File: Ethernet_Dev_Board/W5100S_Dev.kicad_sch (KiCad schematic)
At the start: 41 parts, among them U302 74AUP1T08GWH, Y301 25MHz

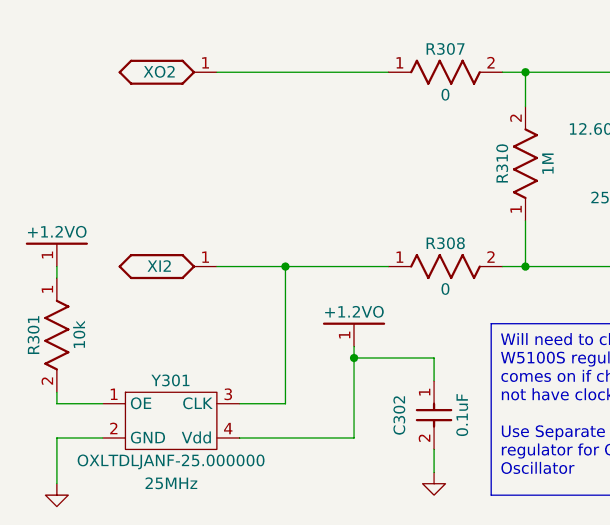
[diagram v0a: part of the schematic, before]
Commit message: Added in 1.2 V regulator and broke out unused IO pins to header
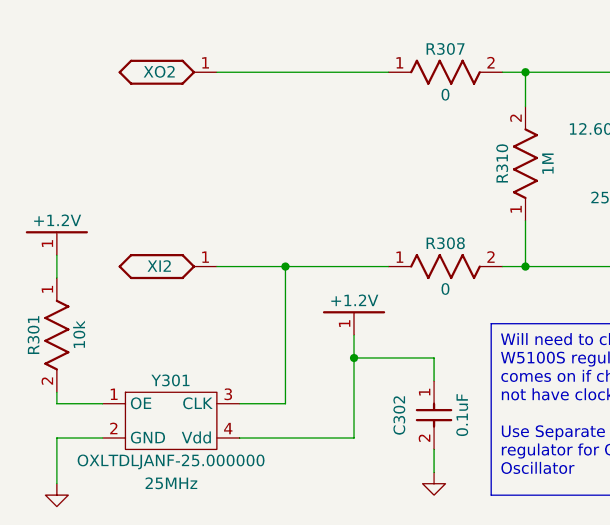
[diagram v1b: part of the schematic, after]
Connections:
- net +1.2VO: no longer C302.1, R301.1, Y301.4 (Vdd)
- new net +1.2V: C302.1, R301.1, Y301.4 (Vdd)
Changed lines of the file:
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@@
 	(wire
 		(pts
-			(xy 50.8 179.07) (xy 50.8 177.8)
+			(xy 50.8 176.53) (xy 50.8 179.07)
 		)
 		(stroke
@@
 	(wire
 		(pts
-			(xy 17.78 170.18) (xy 17.78 168.91)
+			(xy 17.78 167.64) (xy 17.78 170.18)
 		)
 		(stroke
@@
 	)
 	(symbol
+		(lib_id "LED_Controller_Hardware-eagle-import:+3.3V")
+		(at 50.8 177.8 0)
+		(unit 1)
+		(exclude_from_sim no)
+		(in_bom yes)
+		(on_board yes)
+		(dnp no)
+		(property "Reference" "#NetPort0308"
+			(at 50.8 177.8 0)
+			(effects
+				(font
+					(size 1.27 1.27)
+				)
+				(hide yes)
+			)
+		)
+		(property "Value" "+1.2V"
+			(at 50.8 172.72 0)
+			(effects
+				(font
+					(size 1.27 1.27)
+				)
+			)
+		)
+		(property "Footprint" ""
+			(at 50.8 177.8 0)
+			(effects
+				(font
+					(size 1.27 1.27)
+				)
+				(hide yes)
+			)
+		)
+		(property "Datasheet" ""
+			(at 50.8 177.8 0)
+			(effects
+				(font
+					(size 1.27 1.27)
+				)
+				(hide yes)
+			)
+		)
+		(property "Description" ""
+			(at 50.8 177.8 0)
+			(effects
+				(font
+					(size 1.27 1.27)
+				)
+				(hide yes)
+			)
+		)
+		(property "Mfg." ""
+			(at 50.8 177.8 0)
+			(effects
+				(font
+					(size 1.27 1.27)
+				)
+				(hide yes)
+			)
+		)
+		(property "Mfg. PN" ""
+			(at 50.8 177.8 0)
+			(effects
+				(font
+					(size 1.27 1.27)
+				)
+				(hide yes)
+			)
+		)
+		(property "Distributor" ""
+			(at 50.8 177.8 0)
+			(effects
+				(font
+					(size 1.27 1.27)
+				)
+				(hide yes)
+			)
+		)
+		(property "Distributor PN" ""
+			(at 50.8 177.8 0)
+			(effects
+				(font
+					(size 1.27 1.27)
+				)
+				(hide yes)
+			)
+		)
+		(pin "1"
+		)
+		(instances
+			(project "Ethernet_Dev_Board"
+				(path "/79118fbd-6cbf-48b1-af39-9f7b00f17642/e515d953-e2e5-40ce-8d77-bb09cabdad3d"
+					(reference "#NetPort0308")
+					(unit 1)
+				)
+			)
+		)
+	)
+	(symbol
 		(lib_id "LED_Controller_Hardware-eagle-import:ETH_EN")
 		(at 36.83 97.79 180)
@@
 	)
 	(symbol
-		(lib_id "LED_Controller_Hardware-eagle-import:+3.3VA")
-		(at 17.78 170.18 0)
-		(unit 1)
-		(exclude_from_sim no)
-		(in_bom yes)
-		(on_board yes)
-		(dnp no)
-		(property "Reference" "#NetPort0301"
-			(at 17.78 170.18 0)
-			(effects
-				(font
-					(size 1.27 1.27)
-				)
-				(hide yes)
-			)
-		)
-		(property "Value" "+1.2VO"
-			(at 17.78 165.1 0)
-			(effects
-				(font
-					(size 1.27 1.27)
-				)
-			)
-		)
-		(property "Footprint" ""
-			(at 17.78 170.18 0)
-			(effects
-				(font
-					(size 1.27 1.27)
-				)
-				(hide yes)
-			)
-		)
-		(property "Datasheet" ""
-			(at 17.78 170.18 0)
-			(effects
-				(font
-					(size 1.27 1.27)
-				)
-				(hide yes)
-			)
-		)
-		(property "Description" ""
-			(at 17.78 170.18 0)
-			(effects
-				(font
-					(size 1.27 1.27)
-				)
-				(hide yes)
-			)
-		)
-		(property "Mfg." ""
-			(at 17.78 170.18 0)
-			(effects
-				(font
-					(size 1.27 1.27)
-				)
-				(hide yes)
-			)
-		)
-		(property "Mfg. PN" ""
-			(at 17.78 170.18 0)
-			(effects
-				(font
-					(size 1.27 1.27)
-				)
-				(hide yes)
-			)
-		)
-		(property "Distributor" ""
-			(at 17.78 170.18 0)
-			(effects
-				(font
-					(size 1.27 1.27)
-				)
-				(hide yes)
-			)
-		)
-		(property "Distributor PN" ""
-			(at 17.78 170.18 0)
-			(effects
-				(font
-					(size 1.27 1.27)
-				)
-				(hide yes)
-			)
-		)
-		(pin "1"
-		)
-		(instances
-			(project "Ethernet_Dev_Board"
-				(path "/79118fbd-6cbf-48b1-af39-9f7b00f17642/e515d953-e2e5-40ce-8d77-bb09cabdad3d"
-					(reference "#NetPort0301")
-					(unit 1)
-				)
-			)
-		)
-	)
-	(symbol
 		(lib_id "power:GNDS")
 		(at 96.52 165.1 0)
@@
 	(symbol
 		(lib_id "LED_Controller_Hardware-eagle-import:+3.3VA")
-		(at 50.8 179.07 0)
-		(unit 1)
-		(exclude_from_sim no)
-		(in_bom yes)
-		(on_board yes)
-		(dnp no)
-		(property "Reference" "#NetPort0308"
-			(at 50.8 179.07 0)
-			(effects
-				(font
-					(size 1.27 1.27)
-				)
-				(hide yes)
-			)
-		)
-		(property "Value" "+1.2VO"
-			(at 50.8 173.99 0)
-			(effects
-				(font
-					(size 1.27 1.27)
-				)
-			)
-		)
-		(property "Footprint" ""
-			(at 50.8 179.07 0)
-			(effects
-				(font
-					(size 1.27 1.27)
-				)
-				(hide yes)
-			)
-		)
-		(property "Datasheet" ""
-			(at 50.8 179.07 0)
-			(effects
-				(font
-					(size 1.27 1.27)
-				)
-				(hide yes)
-			)
-		)
-		(property "Description" ""
-			(at 50.8 179.07 0)
-			(effects
-				(font
-					(size 1.27 1.27)
-				)
-				(hide yes)
-			)
-		)
-		(property "Mfg." ""
-			(at 50.8 179.07 0)
-			(effects
-				(font
-					(size 1.27 1.27)
-				)
-				(hide yes)
-			)
-		)
-		(property "Mfg. PN" ""
-			(at 50.8 179.07 0)
-			(effects
-				(font
-					(size 1.27 1.27)
-				)
-				(hide yes)
-			)
-		)
-		(property "Distributor" ""
-			(at 50.8 179.07 0)
-			(effects
-				(font
-					(size 1.27 1.27)
-				)
-				(hide yes)
-			)
-		)
-		(property "Distributor PN" ""
-			(at 50.8 179.07 0)
-			(effects
-				(font
-					(size 1.27 1.27)
-				)
-				(hide yes)
-			)
-		)
-		(pin "1"
-		)
-		(instances
-			(project "Ethernet_Dev_Board"
-				(path "/79118fbd-6cbf-48b1-af39-9f7b00f17642/e515d953-e2e5-40ce-8d77-bb09cabdad3d"
-					(reference "#NetPort0308")
-					(unit 1)
-				)
-			)
-		)
-	)
-	(symbol
-		(lib_id "LED_Controller_Hardware-eagle-import:+3.3VA")
 		(at 200.66 69.85 0)
 		(unit 1)
@@
 					(unit 1)
 				)
+			)
+		)
+	)
+	(symbol
+		(lib_id "LED_Controller_Hardware-eagle-import:+3.3V")
+		(at 17.78 168.91 0)
+		(unit 1)
+		(exclude_from_sim no)
+		(in_bom yes)
+		(on_board yes)
+		(dnp no)
+		(property "Reference" "#NetPort0301"
+			(at 17.78 168.91 0)
+			(effects
+				(font
+					(size 1.27 1.27)
+				)
+				(hide yes)
+			)
+		)
+		(property "Value" "+1.2V"
+			(at 17.78 163.83 0)
+			(effects
+				(font
+					(size 1.27 1.27)
+				)
+			)
+		)
+		(property "Footprint" ""
+			(at 17.78 168.91 0)
+			(effects
+				(font
+					(size 1.27 1.27)
+				)
+				(hide yes)
+			)
+		)
+		(property "Datasheet" ""
+			(at 17.78 168.91 0)
+			(effects
+				(font
+					(size 1.27 1.27)
+				)
+				(hide yes)
+			)
+		)
+		(property "Description" ""
+			(at 17.78 168.91 0)
+			(effects
+				(font
+					(size 1.27 1.27)
+				)
+				(hide yes)
+			)
+		)
+		(property "Mfg." ""
+			(at 17.78 168.91 0)
+			(effects
+				(font
+					(size 1.27 1.27)
+				)
+				(hide yes)
+			)
+		)
+		(property "Mfg. PN" ""
+			(at 17.78 168.91 0)
+			(effects
+				(font
+					(size 1.27 1.27)
+				)
+				(hide yes)
+			)
+		)
+		(property "Distributor" ""
+			(at 17.78 168.91 0)
+			(effects
+				(font
+					(size 1.27 1.27)
+				)
+				(hide yes)
+			)
+		)
+		(property "Distributor PN" ""
+			(at 17.78 168.91 0)
+			(effects
+				(font
+					(size 1.27 1.27)
+				)
+				(hide yes)
+			)
+		)
+		(pin "1"
+		)
+		(instances
+			(project "Ethernet_Dev_Board"
+				(path "/79118fbd-6cbf-48b1-af39-9f7b00f17642/e515d953-e2e5-40ce-8d77-bb09cabdad3d"
+					(reference "#NetPort0301")
+					(unit 1)
+				)

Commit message: Net adjustments. Beginning board layout
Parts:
- LED301: value ACTLED -> 5100 ACT
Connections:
- net GNDS: no longer C301.2, C302.2, C303.2, C304.2, C305.2, C306.2, C307.2, C308.2, C309.2, C310.2, C311.2, C312.2, C313.2, R318.1, U301.1 (GNDA), U301.10 (GND), U301.23 (GND), U301.25 (MOD[0]), U301.26 (MOD[1]), U301.27 (MOD[2]), U301.28 (MOD[3]), U301.46 (GND), U301.7 (GNDA), U302.3 (GND), Y301.2 (GND)
- net TX51_P: now reaches R303.2, R309.2, R314.1
- net TXO_P: now reaches R314.2, U301.3 (TXOP)
- net TX51_N: now reaches R302.2, R306.2, R313.1
- net TXO_N: now reaches R313.2, U301.2 (TXON)
- net RX51_N: now reaches R304.2, R311.2, R315.1
- net RXI_N: now reaches R315.2, U301.5 (RXIN)
- net RXI_P: now reaches R316.2, U301.6 (RXIP)
- net RX51_P: now reaches R305.2, R312.2, R316.1
- net RXN_ETH renamed ETH_RX_N
- net RXP_ETH renamed ETH_RX_P
- net TXN_ETH renamed ETH_TX_N
- net TXP_ETH renamed ETH_TX_P
- new net GND1: C301.2, C302.2, C303.2, C304.2, C305.2, C306.2, C307.2, C308.2, C309.2, C310.2, C311.2, C312.2, C313.2, R318.1, U301.1 (GNDA), U301.10 (GND), U301.23 (GND), U301.25 (MOD[0]), U301.26 (MOD[1]), U301.27 (MOD[2]), U301.28 (MOD[3]), U301.46 (GND), U301.7 (GNDA), U302.3 (GND), Y301.2 (GND)
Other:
- moved on the sheet: C301, R313, R314, R315, R316

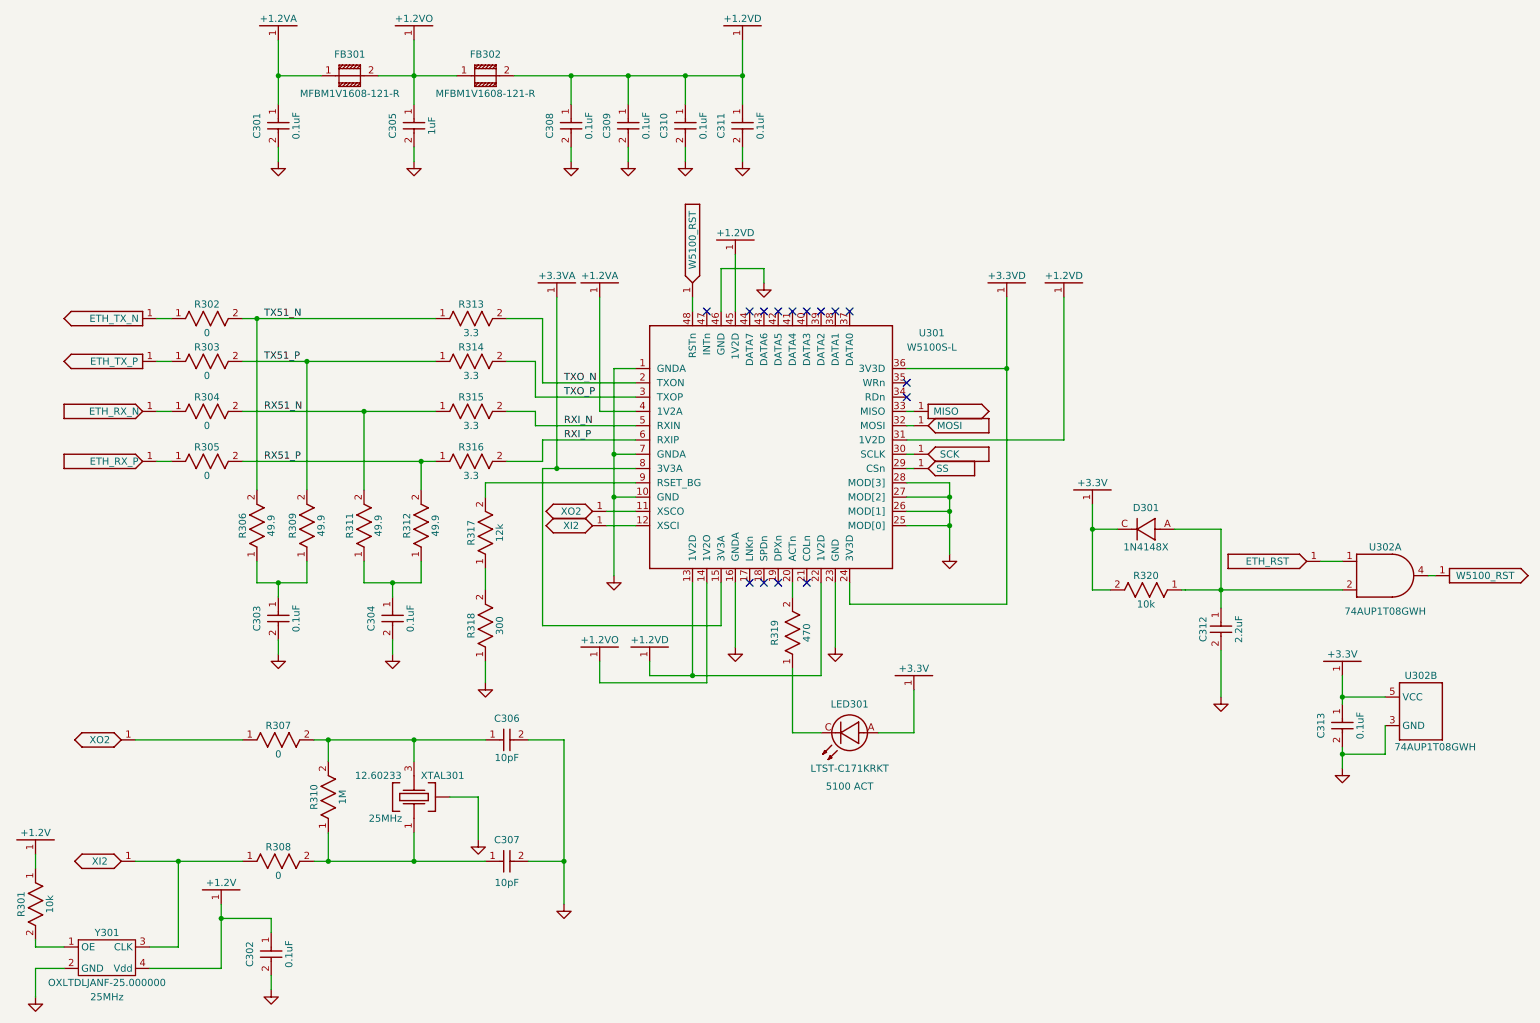
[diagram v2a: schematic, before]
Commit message: Removed 1 TVS diode. removed 1 reset circuit. Placed Ethernet port in both W5500 and W5100S circuits
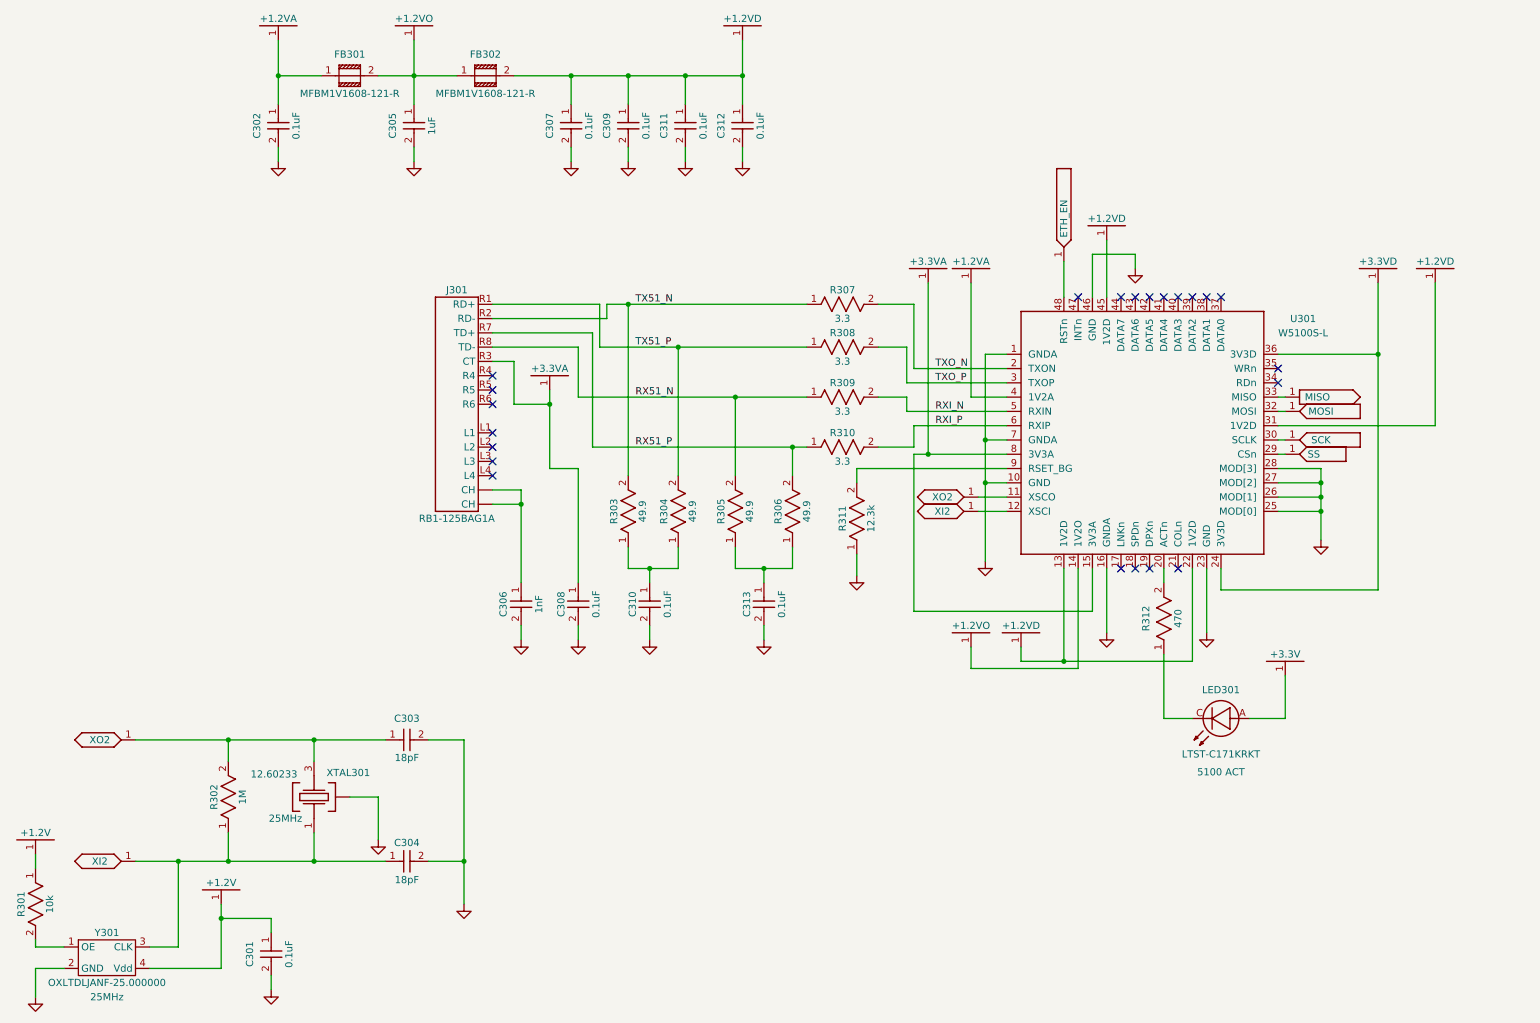
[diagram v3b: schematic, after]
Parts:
- removed C312: 2.2uF, RG_Capacitors_SMD:0603, symbol LED_Controller_Hardware-eagle-import:CAP-0603
- removed C313: 0.1uF, RG_Capacitors_SMD:0603, symbol LED_Controller_Hardware-eagle-import:CAP-0603
- removed D301: 1N4148X, RG_Diode:SOD-523-D, symbol LED_Controller_Hardware-eagle-import:1N4148X
- removed R302, R303, R304, R305, R307, R308: 0, RG_Resistors_SMD:0603, symbol RG_resistors:RES-0603
- removed R318: 300, RG_Resistors_SMD:0603, symbol RG_resistors:RES-0603
- removed R320: 10k, RG_Resistors_SMD:0603, symbol LED_Controller_Hardware-eagle-import:RES-0603
- removed U302: 74AUP1T08GWH, RG_TO_SOT_SMD:SOT23-5P65, symbol RG_Logic:74AUP1T08GWH
- added C306: 1nF, RG_Capacitors_SMD:1206, symbol LED_Controller_Hardware-eagle-import:CAP-1206
- added C308: 0.1uF, RG_Capacitors_SMD:0603, symbol LED_Controller_Hardware-eagle-import:CAP-0603
- added J301: ~, RG_Connectors:WIZNET_RB1-125BAG1A, symbol RG_Connectors:RB1-125BAG1A
- C303: renamed from C306; value 10pF -> 18pF; Distributor PN 1276-1069-2-ND -> 738-CML0603C0G180JT50VTR-ND; Mfg. Samsung Electro-Mechanics -> Stackpole Electronics Inc; Mfg. PN CL10C100CB8NNNC -> CML0603C0G180JT50V
- C304: renamed from C307; value 10pF -> 18pF; Distributor PN 1276-1069-2-ND -> 738-CML0603C0G180JT50VTR-ND; Mfg. Samsung Electro-Mechanics -> Stackpole Electronics Inc; Mfg. PN CL10C100CB8NNNC -> CML0603C0G180JT50V
- R311: renamed from R317; value 12k -> 12.3k; Distributor PN 738-RMCF0603FG12K0TR-ND -> 13-RT0603BRD0712K3LTR-ND; Mfg. Stackpole Electronics Inc -> YAGEO; Mfg. PN RMCF0603FG12K0 -> RT0603BRD0712K3L
- renumbered C302 to C301, C301 to C302, C308 to C307, C303 to C310, C310 to C311, C311 to C312, C304 to C313, R310 to R302, R306 to R303, R309 to R304, R311 to R305, R312 to R306, R313 to R307, R314 to R308, R315 to R309, R316 to R310, R319 to R312
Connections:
- net +3.3VA: now also C308.1, J301.R3 (CT)
- net GND1: now also R311.1, C306.2, C308.2
- net RX51_N: now also J301.R8 (TD-)
- net RX51_P: now also J301.R7 (TD+)
- net TX51_N: now also J301.R2 (RD-)
- net TX51_P: now also J301.R1 (RD+)
- net XI2: now also C304.1, R302.1, XTAL301.1
- net XO2: now also C303.1, R302.2, XTAL301.3 (3@1)
- net W5100_RST renamed ETH_EN
- new net: C306.1, J301.S1 (CH), J301.S2 (CH)
- no-connect marks 15 -> 22
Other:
- moved on the sheet: C303, C304, C310, C313, LED301, R302, R303, R304, R305, R306, R307, R308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

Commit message: Removed unnecessary nets. Beginning board routing
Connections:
- net GNDS is gone; now on net GND1: U301.16 (GNDA), XTAL301.2 (CASE)
- net +3.3V: now also U301.15 (3V3A), U301.8 (3V3A)
- net +3.3VA: no longer U301.15 (3V3A), U301.8 (3V3A)
- net +3.3VD renamed +3.3VA2

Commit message: Finished first version of routing the board. Also adjusted some nets
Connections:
- net +3.3VA is gone; now on net +3.3VA2: C308.1, J301.R3 (CT)
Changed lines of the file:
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@@
 			)
 		)
-		(property "Value" "+3.3VA"
+		(property "Value" "+3.3VA2"
 			(at 109.22 81.28 0)
 			(effects

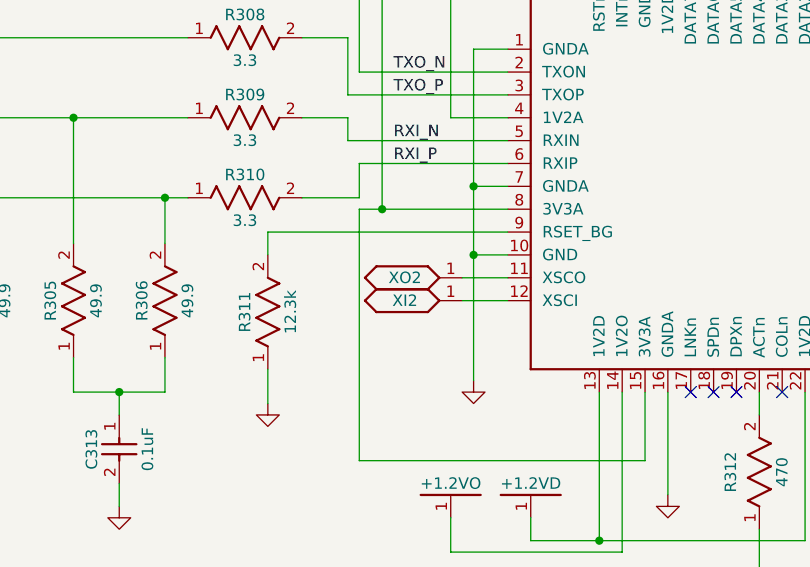
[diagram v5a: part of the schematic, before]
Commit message: Converted Board into 4 layers
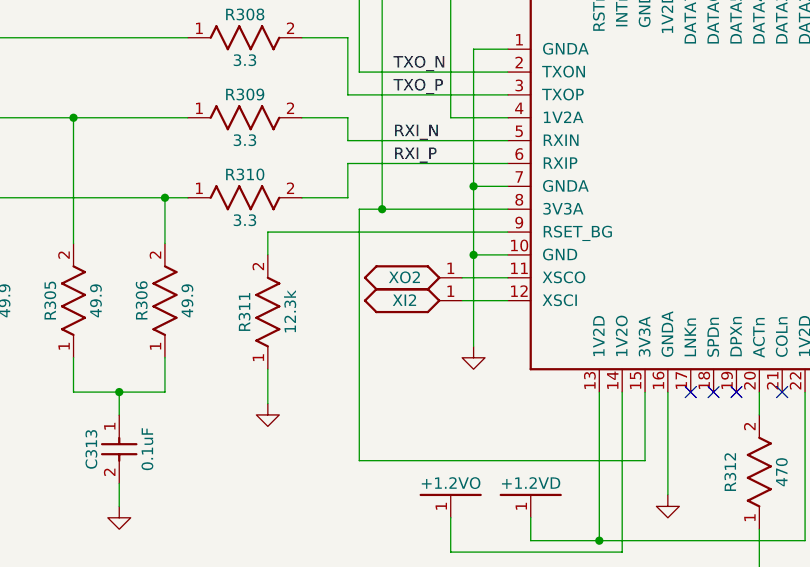
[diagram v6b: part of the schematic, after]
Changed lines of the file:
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@@
 	(wire
 		(pts
-			(xy 173.99 91.44) (xy 173.99 95.25)
+			(xy 172.72 91.44) (xy 172.72 95.25)
 		)
 		(stroke
@@
 	(wire
 		(pts
-			(xy 186.69 101.6) (xy 186.69 115.57)
+			(xy 186.69 101.6) (xy 186.69 111.76)
 		)
 		(stroke
@@
 	(wire
 		(pts
-			(xy 173.99 95.25) (xy 167.64 95.25)
+			(xy 172.72 95.25) (xy 167.64 95.25)
 		)
 		(stroke
@@
 	(wire
 		(pts
-			(xy 190.5 91.44) (xy 173.99 91.44)
+			(xy 190.5 91.44) (xy 172.72 91.44)
 		)
 		(stroke
@@
 	(symbol
 		(lib_id "power:GNDS")
-		(at 186.69 115.57 0)
+		(at 186.69 111.76 0)
 		(unit 1)
 		(exclude_from_sim no)
@@
 		(fields_autoplaced yes)
 		(property "Reference" "#PWR0316"
-			(at 186.69 121.92 0)
+			(at 186.69 118.11 0)
 			(effects
 				(font
@@
 		)
 		(property "Value" "GND1"
-			(at 186.69 120.65 0)
+			(at 186.69 116.84 0)
 			(effects
 				(font
@@
 		)
 		(property "Footprint" ""
-			(at 186.69 115.57 0)
+			(at 186.69 111.76 0)
 			(effects
 				(font
@@
 		)
 		(property "Datasheet" ""
-			(at 186.69 115.57 0)
+			(at 186.69 111.76 0)
 			(effects
 				(font
@@
 		)
 		(property "Description" "Power symbol creates a global label with name \"GNDS\" , signal ground"
-			(at 186.69 115.57 0)
+			(at 186.69 111.76 0)
 			(effects
 				(font
@@
 		)
 		(property "Mfg." ""
-			(at 186.69 115.57 0)
+			(at 186.69 111.76 0)
 			(effects
 				(font
@@
 		)
 		(property "Mfg. PN" ""
-			(at 186.69 115.57 0)
+			(at 186.69 111.76 0)
 			(effects
 				(font
@@
 		)
 		(property "Distributor" ""
-			(at 186.69 115.57 0)
+			(at 186.69 111.76 0)
 			(effects
 				(font
@@
 		)
 		(property "Distributor PN" ""
-			(at 186.69 115.57 0)
+			(at 186.69 111.76 0)
 			(effects
 				(font
